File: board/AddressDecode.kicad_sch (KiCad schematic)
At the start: 18 parts, among them U10 74LS154, U11 74F00, U12 74F02, U13 74F08, U14 74F32, U15 74F30, U16 74LS260, U17 74LS154, U18 7404

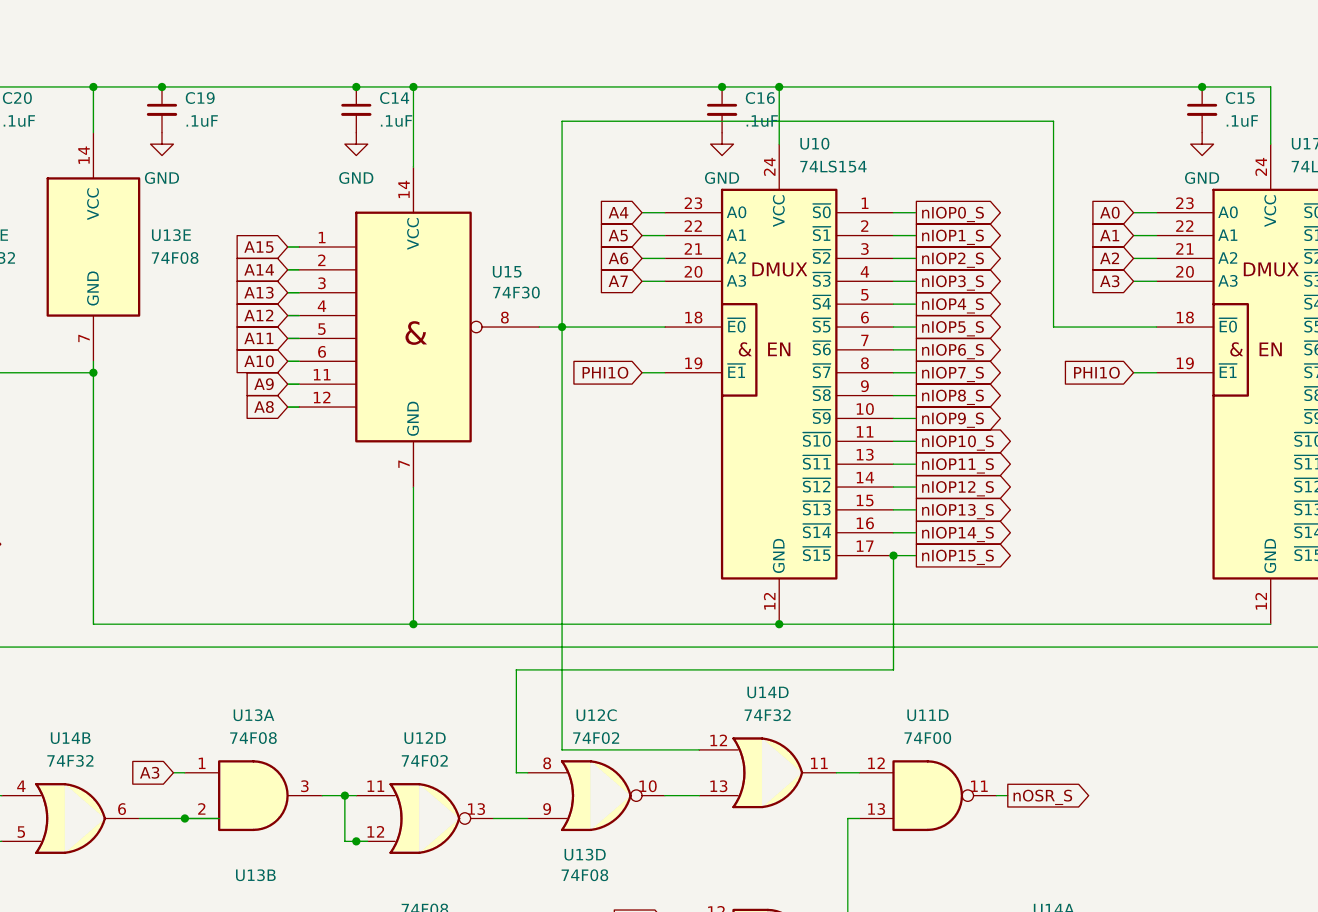
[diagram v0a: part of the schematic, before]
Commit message: Added clocks and power connector.
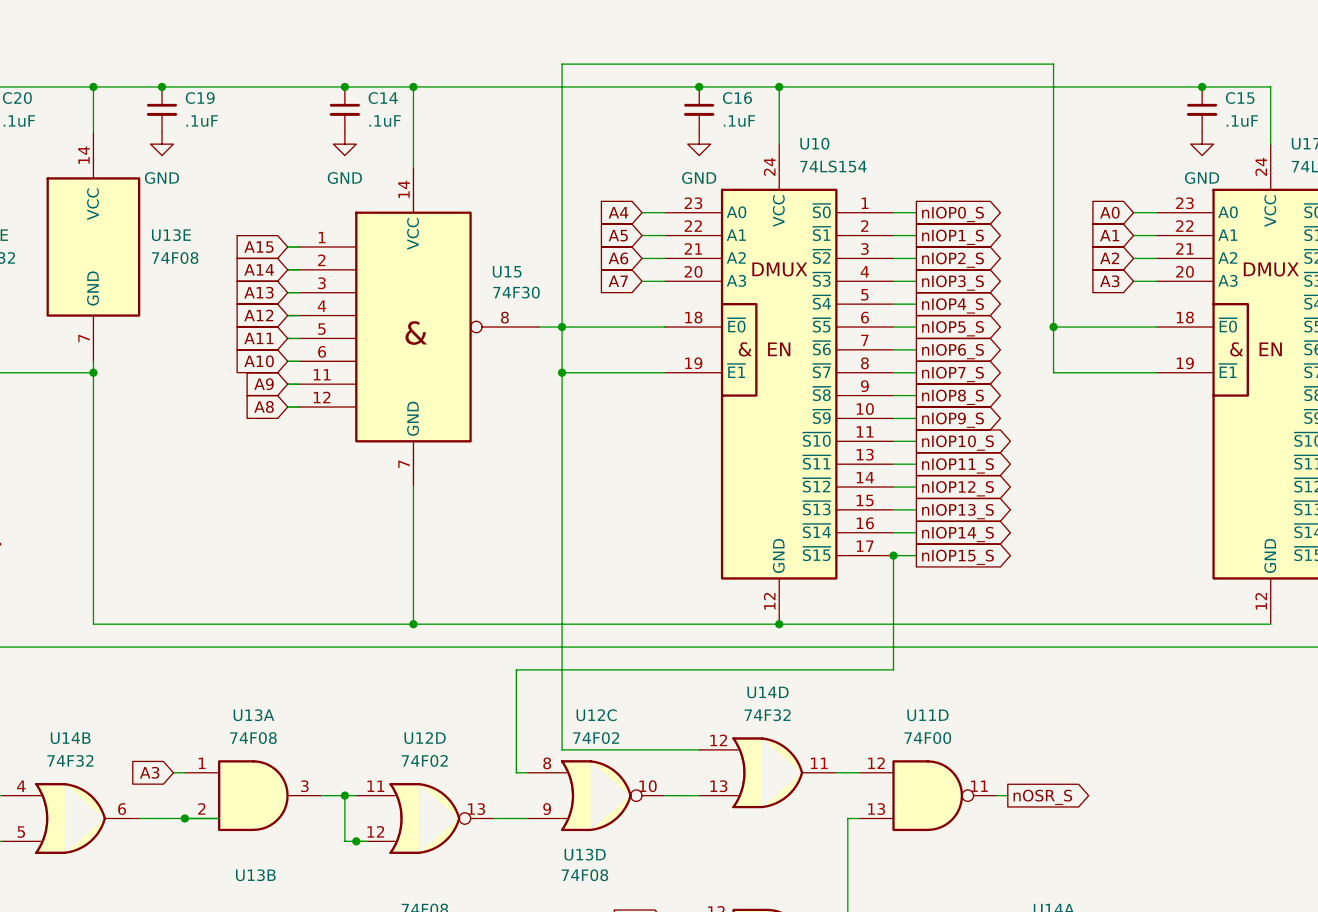
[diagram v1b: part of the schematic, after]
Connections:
- net PHI1O is gone; now on an unnamed net: U10.19 (~{E1}), U17.19 (~{E1})
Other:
- moved on the sheet: C14, C16
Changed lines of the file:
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@@
 	)
 	(junction
+		(at 158.75 57.15)
+		(diameter 0)
+		(color 0 0 0 0)
+	)
+	(junction
 		(at 31.75 25.4)
 		(diameter 0)
@@
 	)
 	(junction
+		(at 213.36 52.07)
+		(diameter 0)
+		(color 0 0 0 0)
+	)
+	(junction
 		(at 255.27 120.65)
 		(diameter 0)
@@
 	)
 	(junction
-		(at 176.53 25.4)
+		(at 173.99 25.4)
 		(diameter 0)
 		(color 0 0 0 0)
@@
 	)
 	(junction
-		(at 135.89 25.4)
+		(at 134.62 25.4)
 		(diameter 0)
 		(color 0 0 0 0)
@@
 	(wire
 		(pts
-			(xy 222.25 57.15) (xy 224.79 57.15)
+			(xy 198.12 52.07) (xy 195.58 52.07)
 		)
 		(stroke
@@
 	(wire
 		(pts
-			(xy 198.12 52.07) (xy 195.58 52.07)
+			(xy 134.62 120.65) (xy 135.89 120.65)
 		)
 		(stroke
@@
 	(wire
 		(pts
-			(xy 134.62 120.65) (xy 135.89 120.65)
+			(xy 213.36 57.15) (xy 224.79 57.15)
 		)
 		(stroke
@@
 	(wire
 		(pts
-			(xy 142.24 25.4) (xy 176.53 25.4)
+			(xy 142.24 25.4) (xy 173.99 25.4)
 		)
 		(stroke
@@
 	(wire
 		(pts
-			(xy 135.89 25.4) (xy 142.24 25.4)
+			(xy 134.62 25.4) (xy 142.24 25.4)
 		)
 		(stroke
@@
 	(wire
 		(pts
-			(xy 158.75 99.06) (xy 158.75 52.07)
+			(xy 213.36 52.07) (xy 213.36 57.15)
 		)
 		(stroke
@@
 	(wire
 		(pts
-			(xy 128.27 50.8) (xy 129.54 50.8)
+			(xy 158.75 99.06) (xy 158.75 57.15)
 		)
 		(stroke
@@
 	(wire
 		(pts
-			(xy 130.81 125.73) (xy 132.08 125.73)
+			(xy 128.27 50.8) (xy 129.54 50.8)
 		)
 		(stroke
@@
 	(wire
 		(pts
-			(xy 255.27 130.81) (xy 255.27 120.65)
+			(xy 130.81 125.73) (xy 132.08 125.73)
 		)
 		(stroke
@@
 	(wire
 		(pts
-			(xy 252.73 69.85) (xy 250.19 69.85)
+			(xy 255.27 130.81) (xy 255.27 120.65)
 		)
 		(stroke
@@
 	(wire
 		(pts
-			(xy 167.64 57.15) (xy 170.18 57.15)
+			(xy 252.73 69.85) (xy 250.19 69.85)
 		)
 		(stroke
@@
 	(wire
 		(pts
-			(xy 213.36 52.07) (xy 213.36 29.21)
+			(xy 213.36 52.07) (xy 213.36 22.86)
 		)
 		(stroke
@@
 	(wire
 		(pts
-			(xy 176.53 25.4) (xy 182.88 25.4)
+			(xy 173.99 25.4) (xy 182.88 25.4)
 		)
 		(stroke
@@
 	(wire
 		(pts
+			(xy 158.75 57.15) (xy 170.18 57.15)
+		)
+		(stroke
+			(width 0)
+			(type default)
+		)
+	)
+	(wire
+		(pts
 			(xy 167.64 44.45) (xy 170.18 44.45)
 		)
@@
 	(wire
 		(pts
-			(xy 213.36 29.21) (xy 158.75 29.21)
+			(xy 213.36 22.86) (xy 158.75 22.86)
 		)
 		(stroke
@@
 	(wire
 		(pts
+			(xy 158.75 57.15) (xy 158.75 52.07)
+		)
+		(stroke
+			(width 0)
+			(type default)
+		)
+	)
+	(wire
+		(pts
 			(xy 66.04 25.4) (xy 66.04 30.48)
 		)
@@
 	(wire
 		(pts
-			(xy 158.75 29.21) (xy 158.75 52.07)
+			(xy 158.75 22.86) (xy 158.75 52.07)
 		)
 		(stroke
@@
 	(wire
 		(pts
-			(xy 114.3 25.4) (xy 135.89 25.4)
+			(xy 114.3 25.4) (xy 134.62 25.4)
 		)
 		(stroke
@@
 		)
 	)
-	(global_label "PHI1O"
-		(shape input)
-		(at 167.64 57.15 180)
-		(fields_autoplaced yes)
-		(effects
-			(font
-				(size 1.27 1.27)
-			)
-			(justify right)
-		)
-		(property "Intersheetrefs" "${INTERSHEET_REFS}"
-			(at 158.9095 57.15 0)
-			(effects
-				(font
-					(size 1.27 1.27)
-				)
-				(justify right)
-				(hide yes)
-			)
-		)
-	)
 	(global_label "A14"
 		(shape input)
@@
 		)
 	)
-	(global_label "PHI1O"
-		(shape input)
-		(at 222.25 57.15 180)
-		(fields_autoplaced yes)
-		(effects
-			(font
-				(size 1.27 1.27)
-			)
-			(justify right)
-		)
-		(property "Intersheetrefs" "${INTERSHEET_REFS}"
-			(at 213.5195 57.15 0)
-			(effects
-				(font
-					(size 1.27 1.27)
-				)
-				(justify right)
-				(hide yes)
-			)
-		)
-	)
 	(global_label "nIOB15_S"
 		(shape output)
@@
 	(symbol
 		(lib_id "power:GND")
-		(at 176.53 30.48 0)
+		(at 173.99 30.48 0)
 		(unit 1)
 		(exclude_from_sim no)
@@
 		(fields_autoplaced yes)
 		(property "Reference" "#PWR019"
-			(at 176.53 36.83 0)
+			(at 173.99 36.83 0)
 			(effects
 				(font
@@
 		)
 		(property "Value" "GND"
-			(at 176.53 35.56 0)
+			(at 173.99 35.56 0)
 			(effects
 				(font
@@
 		)
 		(property "Footprint" ""
-			(at 176.53 30.48 0)
+			(at 173.99 30.48 0)
 			(effects
 				(font
@@
 		)
 		(property "Datasheet" ""
-			(at 176.53 30.48 0)
+			(at 173.99 30.48 0)
 			(effects
 				(font
@@
 		)
 		(property "Description" "Power symbol creates a global label with name \"GND\" , ground"
-			(at 176.53 30.48 0)
+			(at 173.99 30.48 0)
 			(effects
 				(font
@@
 	(symbol
 		(lib_id "Device:C_Small")
-		(at 135.89 27.94 0)
+		(at 134.62 27.94 0)
 		(unit 1)
 		(exclude_from_sim no)
@@
 		(fields_autoplaced yes)
 		(property "Reference" "C14"
-			(at 138.43 26.6762 0)
+			(at 137.16 26.6762 0)
 			(effects
 				(font
@@
 		)
 		(property "Value" ".1uF"
-			(at 138.43 29.2162 0)
+			(at 137.16 29.2162 0)
 			(effects
 				(font
@@
 		)
 		(property "Footprint" "Capacitor_THT:C_Disc_D5.0mm_W2.5mm_P5.00mm"
-			(at 135.89 27.94 0)
+			(at 134.62 27.94 0)
 			(effects
 				(font
@@
 		)
 		(property "Datasheet" "~"
-			(at 135.89 27.94 0)
+			(at 134.62 27.94 0)
 			(effects
 				(font
@@
 		)
 		(property "Description" "Unpolarized capacitor, small symbol"
-			(at 135.89 27.94 0)
+			(at 134.62 27.94 0)
 			(effects
 				(font
@@
 	(symbol
 		(lib_id "Device:C_Small")
-		(at 176.53 27.94 0)
+		(at 173.99 27.94 0)
 		(unit 1)
 		(exclude_from_sim no)
@@
 		(fields_autoplaced yes)
 		(property "Reference" "C16"
-			(at 179.07 26.6762 0)
+			(at 176.53 26.6762 0)
 			(effects
 				(font
@@
 		)
 		(property "Value" ".1uF"
-			(at 179.07 29.2162 0)
+			(at 176.53 29.2162 0)
 			(effects
 				(font
@@
 		)
 		(property "Footprint" "Capacitor_THT:C_Disc_D5.0mm_W2.5mm_P5.00mm"
-			(at 176.53 27.94 0)
+			(at 173.99 27.94 0)
 			(effects
 				(font
@@
 		)
 		(property "Datasheet" "~"
-			(at 176.53 27.94 0)
+			(at 173.99 27.94 0)
 			(effects
 				(font
@@
 		)
 		(property "Description" "Unpolarized capacitor, small symbol"
-			(at 176.53 27.94 0)
+			(at 173.99 27.94 0)
 			(effects
 				(font
@@
 	(symbol
 		(lib_id "power:GND")
-		(at 135.89 30.48 0)
+		(at 134.62 30.48 0)
 		(unit 1)
 		(exclude_from_sim no)
@@
 		(fields_autoplaced yes)
 		(property "Reference" "#PWR017"
-			(at 135.89 36.83 0)
+			(at 134.62 36.83 0)
 			(effects
 				(font
@@
 		)
 		(property "Value" "GND"
-			(at 135.89 35.56 0)
+			(at 134.62 35.56 0)
 			(effects
 				(font
@@
 		)
 		(property "Footprint" ""
-			(at 135.89 30.48 0)
+			(at 134.62 30.48 0)
 			(effects
 				(font
@@
 		)
 		(property "Datasheet" ""
-			(at 135.89 30.48 0)
+			(at 134.62 30.48 0)
 			(effects
 				(font
@@
 		)
 		(property "Description" "Power symbol creates a global label with name \"GND\" , ground"
-			(at 135.89 30.48 0)
+			(at 134.62 30.48 0)
 			(effects
 				(font

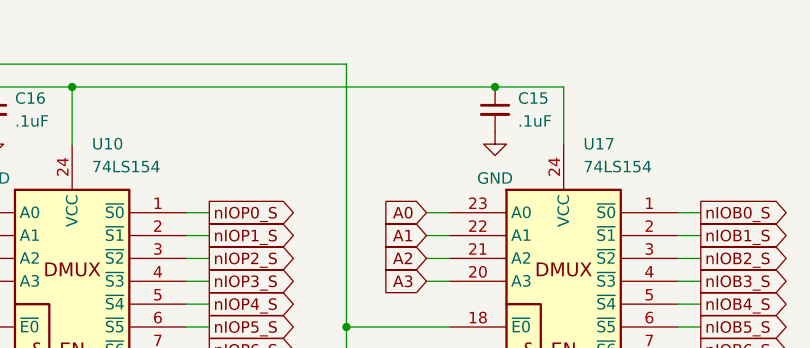
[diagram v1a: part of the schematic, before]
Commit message: Changing to ATX-sized motherboard with 8 62-pin ISA slots.  Other component connection cleanup as well.
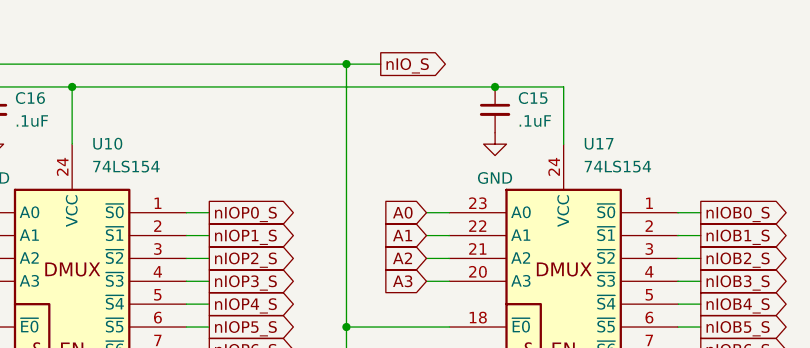
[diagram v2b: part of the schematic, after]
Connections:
- net nIO_S: now reaches U10.18 (~{E0}), U10.19 (~{E1}), U14.12, U15.8, U17.18 (~{E0}), U17.19 (~{E1})
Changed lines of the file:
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@@
 	)
 	(junction
+		(at 213.36 22.86)
+		(diameter 0)
+		(color 0 0 0 0)
+	)
+	(junction
 		(at 153.67 138.43)
 		(diameter 0)
@@
 	(wire
 		(pts
+			(xy 213.36 22.86) (xy 217.17 22.86)
+		)
+		(stroke
+			(width 0)
+			(type default)
+		)
+	)
+	(wire
+		(pts
 			(xy 134.62 120.65) (xy 135.89 120.65)
 		)
@@
 			(effects
 				(font
+					(size 1.27 1.27)
+				)
+				(justify left)
+				(hide yes)
+			)
+		)
+	)
+	(global_label "nIO_S"
+		(shape output)
+		(at 217.17 22.86 0)
+		(fields_autoplaced yes)
+		(effects
+			(font
+				(size 1.27 1.27)
+			)
+			(justify left)
+		)
+		(property "Intersheetrefs" "${INTERSHEET_REFS}"
+			(at 225.4166 22.86 0)
+			(effects
+				(font

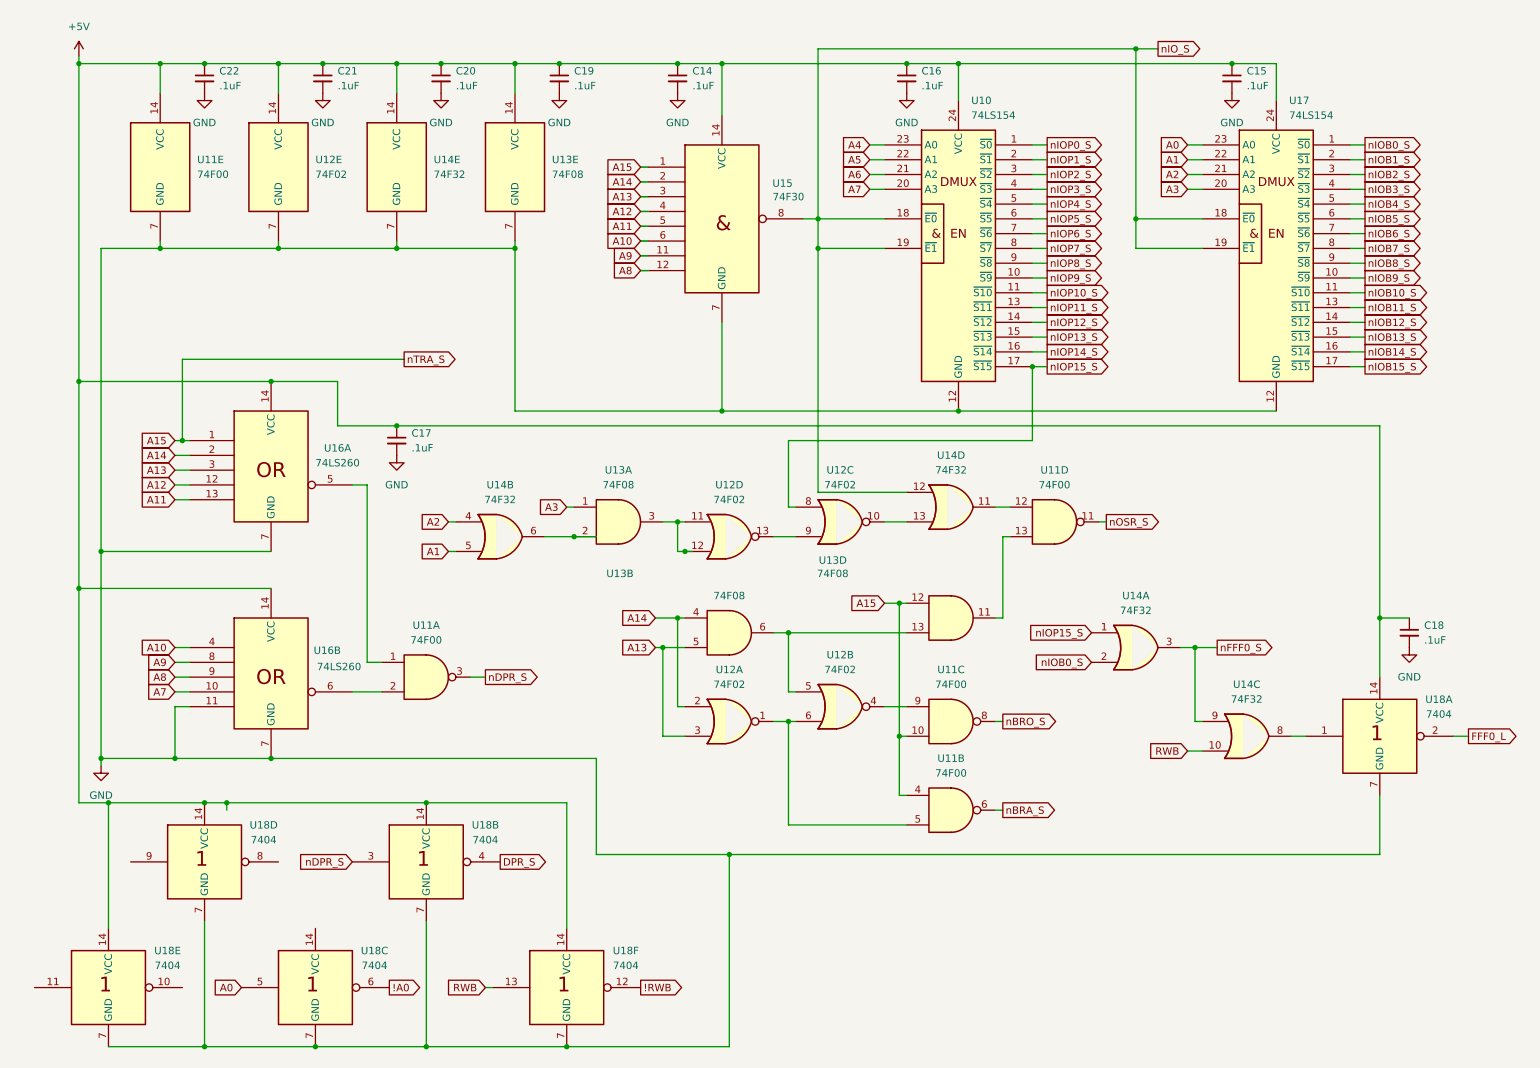
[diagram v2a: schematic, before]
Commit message: Added surface mount version of memory daughter cards, and lots of schematic updates and fixes, including adding dedicated registers for shared memory bank select at $FFF1 and IRQ vTable entry selector at $FFF2 along with the IRQ vTable registers and priority encoders for 16 IRQs
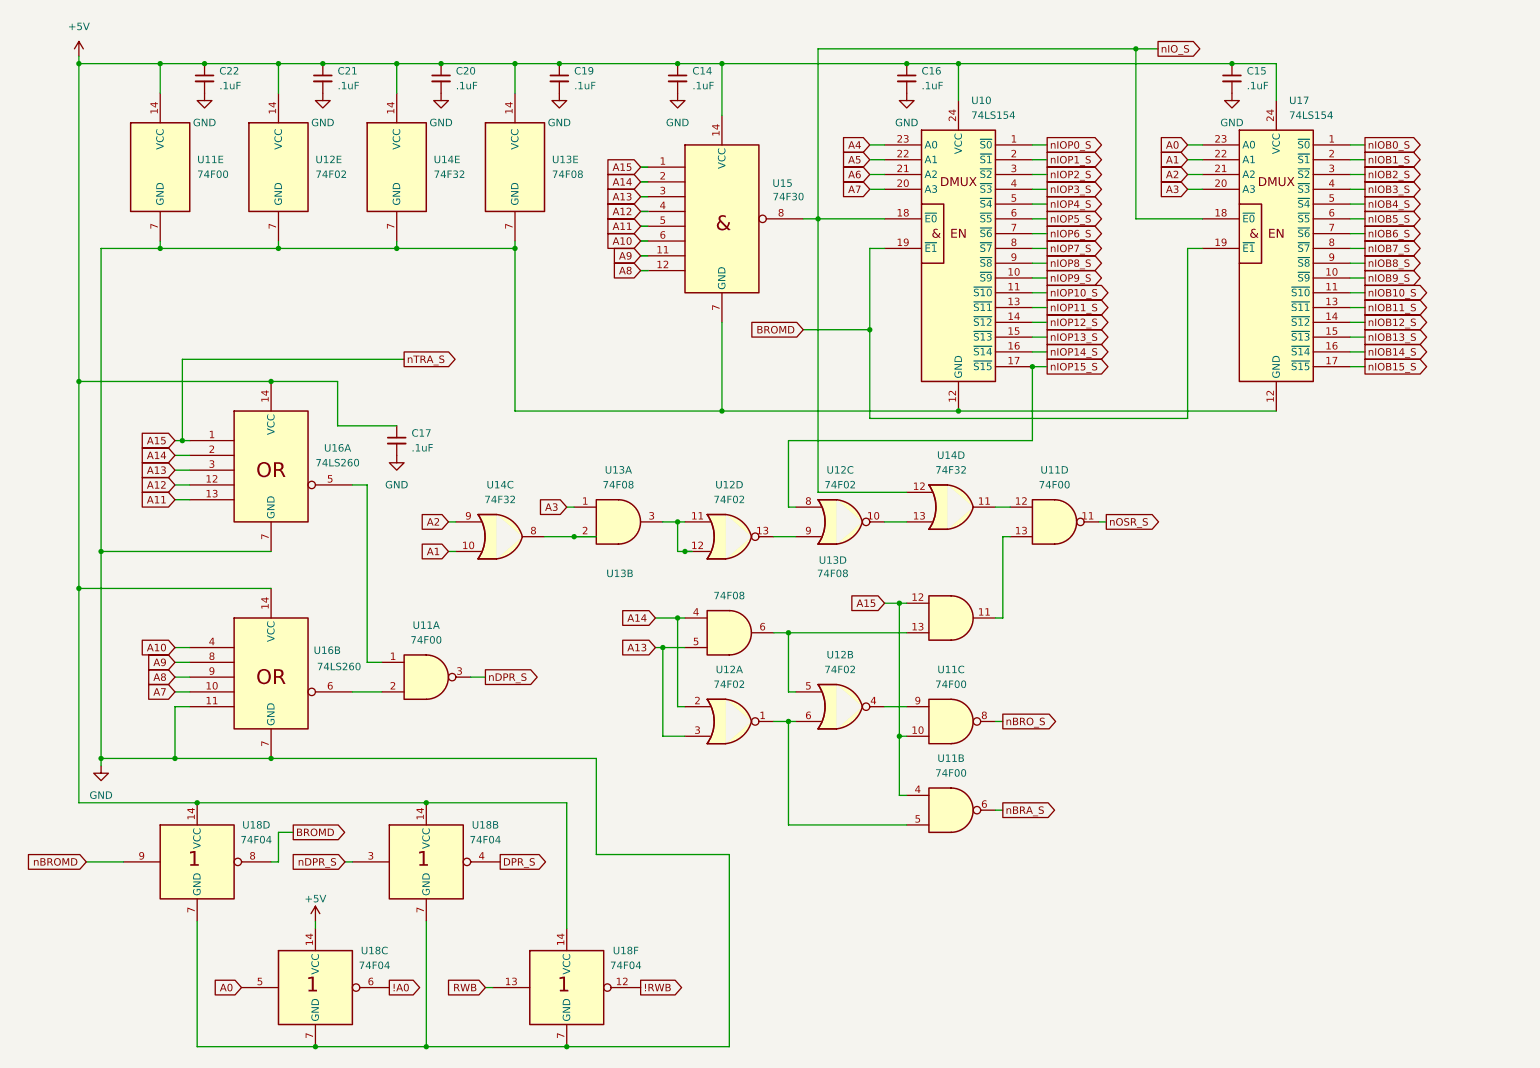
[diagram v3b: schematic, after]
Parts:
- removed C18: .1uF, Capacitor_THT:C_Disc_D5.0mm_W2.5mm_P5.00mm, symbol Device:C_Small
- removed unit 3 of U14
- removed unit 1 of U14
- removed unit 1 of U18
- removed unit 5 of U18
- U18: value 7404 -> 74F04
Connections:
- net +5V: now also U18.14 (VCC)
- net A1: now also U14.10; no longer U14.5
- net A2: now also U14.9; no longer U14.4
- net nIO_S: no longer U10.19 (~{E1}), U17.19 (~{E1})
- net BROMD: now reaches U18.8
- net BROMD: now also U10.19 (~{E1}), U17.19 (~{E1})
- net nBROMD: now reaches U18.9
- net at U13.2: now also U14.8; no longer U14.6
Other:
- moved on the sheet: U18D
